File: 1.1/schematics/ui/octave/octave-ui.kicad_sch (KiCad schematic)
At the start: 7 parts

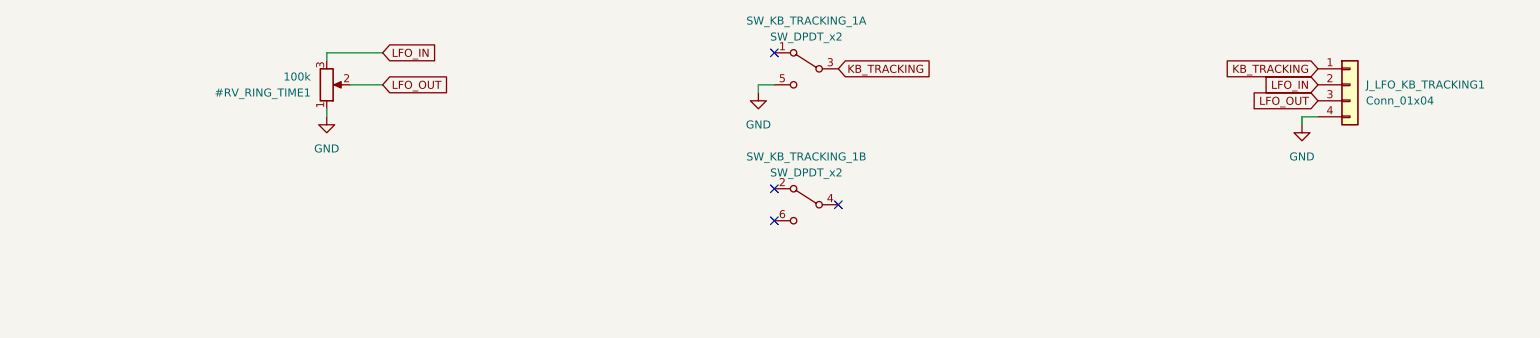
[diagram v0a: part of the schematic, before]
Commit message: Added chord logic (untested)
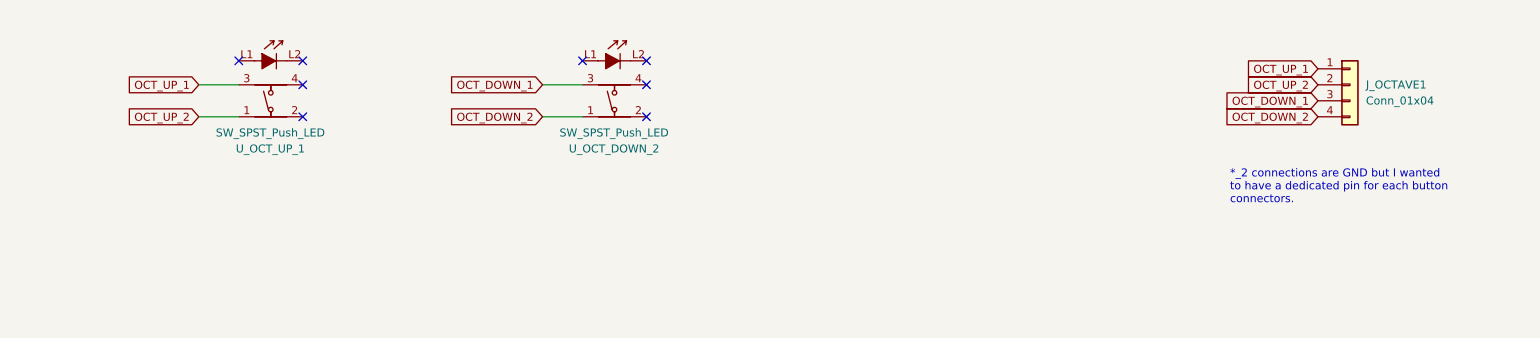
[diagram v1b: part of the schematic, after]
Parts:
- removed #RV_RING_TIME1: 100k, Shmoergh_Custom_Footprints:Potentiometer_Alpha_RD901F-40-00D_Single_Vertical, symbol Device:R_Potentiometer
- removed SW_KB_TRACKING_1: SW_DPDT_x2, Shmoergh_Custom_Footprints:DPDT Korg Style Switch, symbol Shmoergh_Custom_Components:SW_DPDT_x2
- added U_OCT_DOWN_2, U_OCT_UP_1: SW_SPST_Push_LED, Shmoergh_Custom_Footprints:SPST_Narrow_Circular_Pushbutton_LED, symbol Shmoergh_Custom_Components:SW_SPST_Push_LED
- renumbered J_LFO_KB_TRACKING1 to J_OCTAVE1
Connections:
- net GND renamed OCT_DOWN_2
- net OCT_DOWN_2: now also U_OCT_DOWN_2.1
- net KB_TRACKING renamed OCT_UP_1
- net OCT_UP_1: now also U_OCT_UP_1.3
- net LFO_IN renamed OCT_UP_2
- net OCT_UP_2: now also U_OCT_UP_1.1
- net LFO_OUT renamed OCT_DOWN_1
- net OCT_DOWN_1: now also U_OCT_DOWN_2.3
- no-connect marks 4 -> 8
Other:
- note added: "*_2 connections are GND but I wanted to have a dedicated pin for each button connectors."
